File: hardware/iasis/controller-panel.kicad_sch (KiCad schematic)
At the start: 23 parts, among them SW1171 PTS645SL50SMTR92LFS, U1171 SN74AHCT1G125DBVR, U1172 TCA6408ARGTR

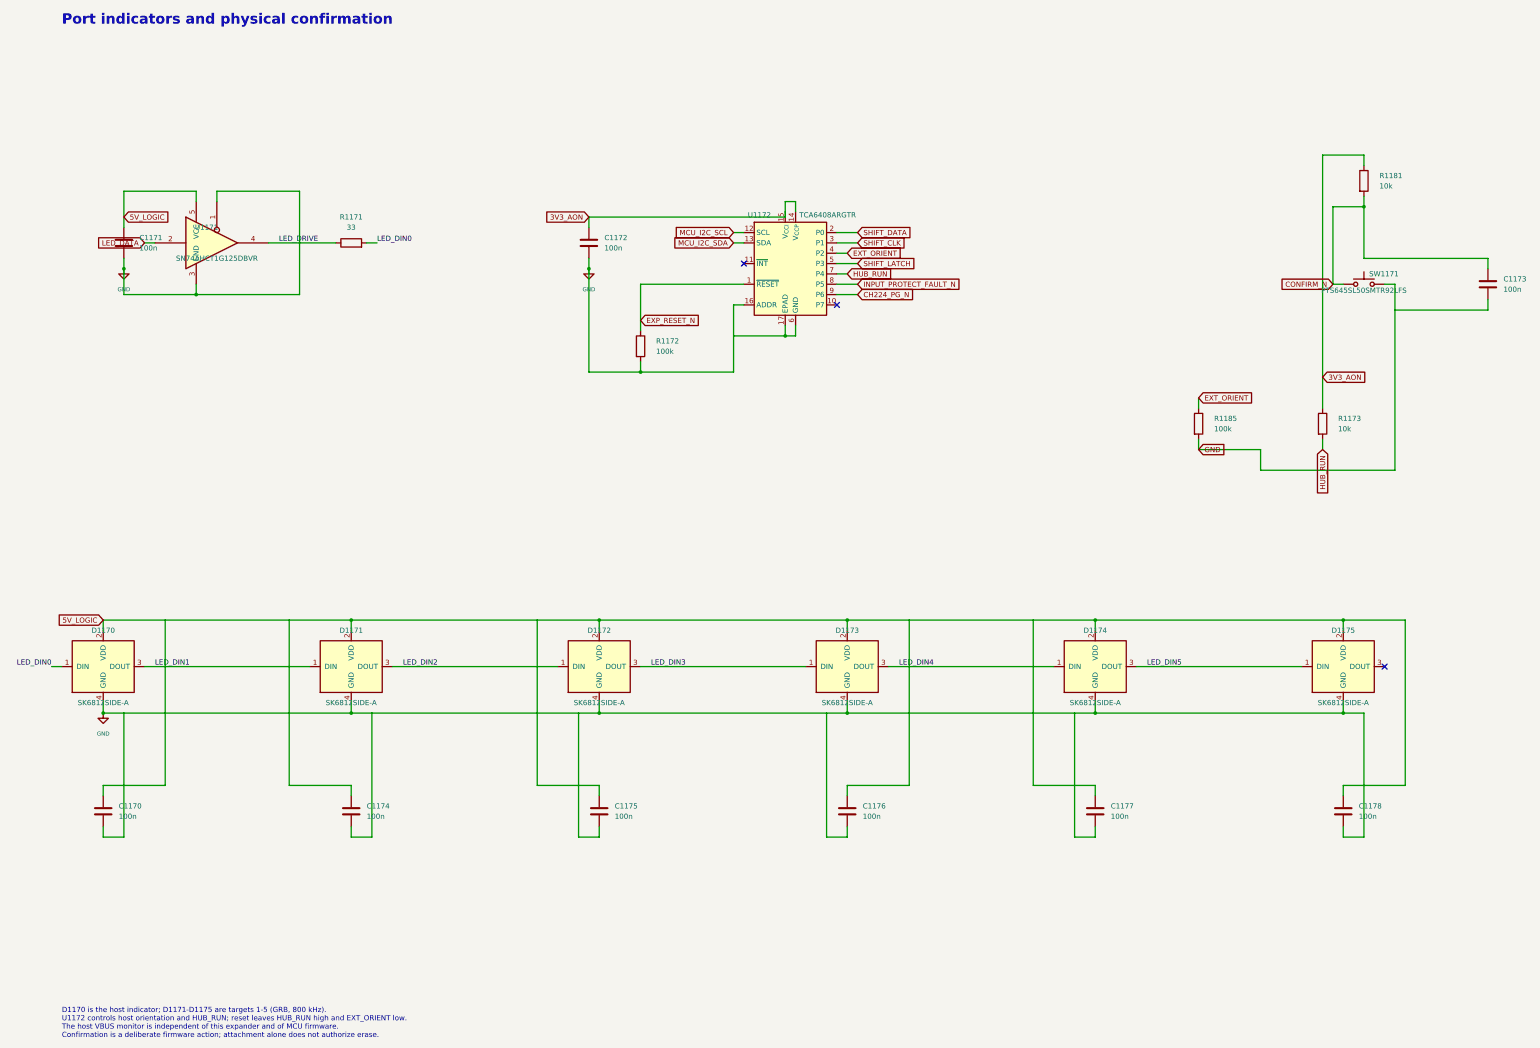
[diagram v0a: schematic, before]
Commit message: Wire the schematic islands and side-match the RP2354 GPIOs
Each sheet now draws its circuits with wires. Labels remain at block edges
and on single-part islands: buttons, test points, decoupling and pull
resistors. The target-port page wires its hierarchical labels straight to
the child sheet pins, the ports page points its labels away from each
block, and the root sheet keeps every block clear of the title block.

The RP2354B GPIOs are reassigned so each signal leaves the package on the
side facing its destination. Update PCB from Schematic applied the 43
U1101 pad-net changes with no geometry change. Otherwise the netlist
matches the previous design, ERC keeps its 14 existing warnings and DRC
reports no parity issues.
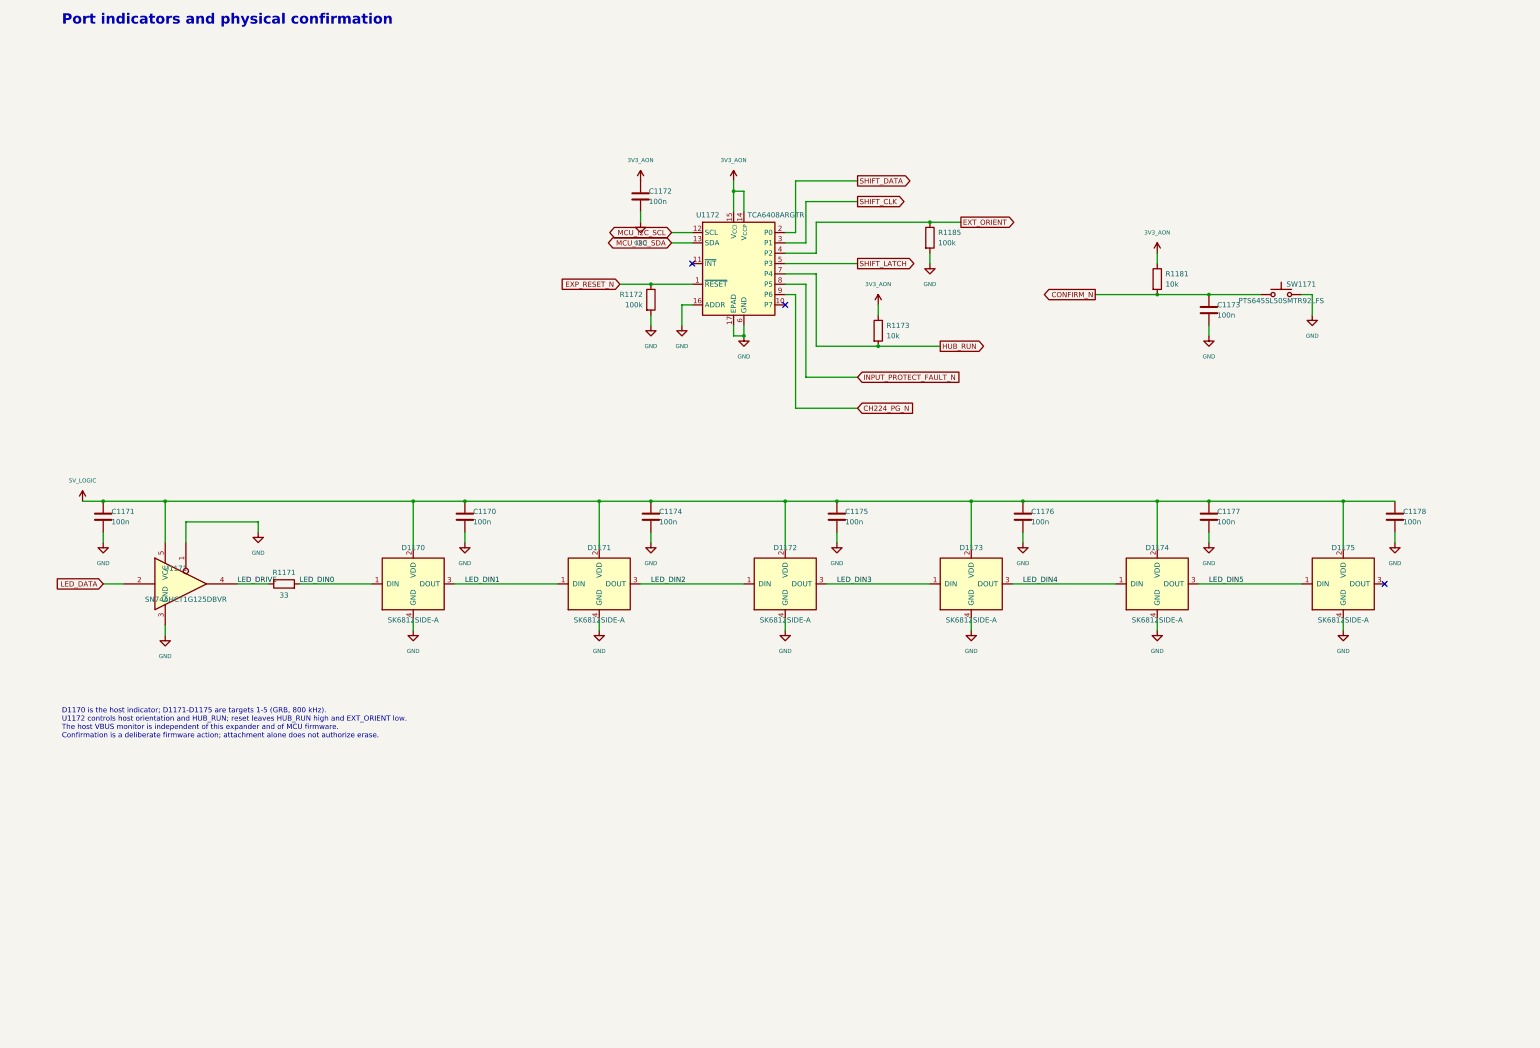
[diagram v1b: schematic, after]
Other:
- moved on the sheet: C1170, C1171, C1172, C1173, C1174, C1175, C1176, C1177, C1178, D1170, D1171, D1172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

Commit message: Redraw the controller support sheets
The management bus, indicator, power-control, voltage-measurement and
temperature sheets read left to right, with supplies up, ground down
and decoupling beside each IC. Pull resistors, test points and buttons
are labelled islands; everything else is wired. Supply rails use power
symbols with their existing net names, fields sit clear of bodies,
wires and text, and each sheet carries a title, date and revision. The
netlist is unchanged.
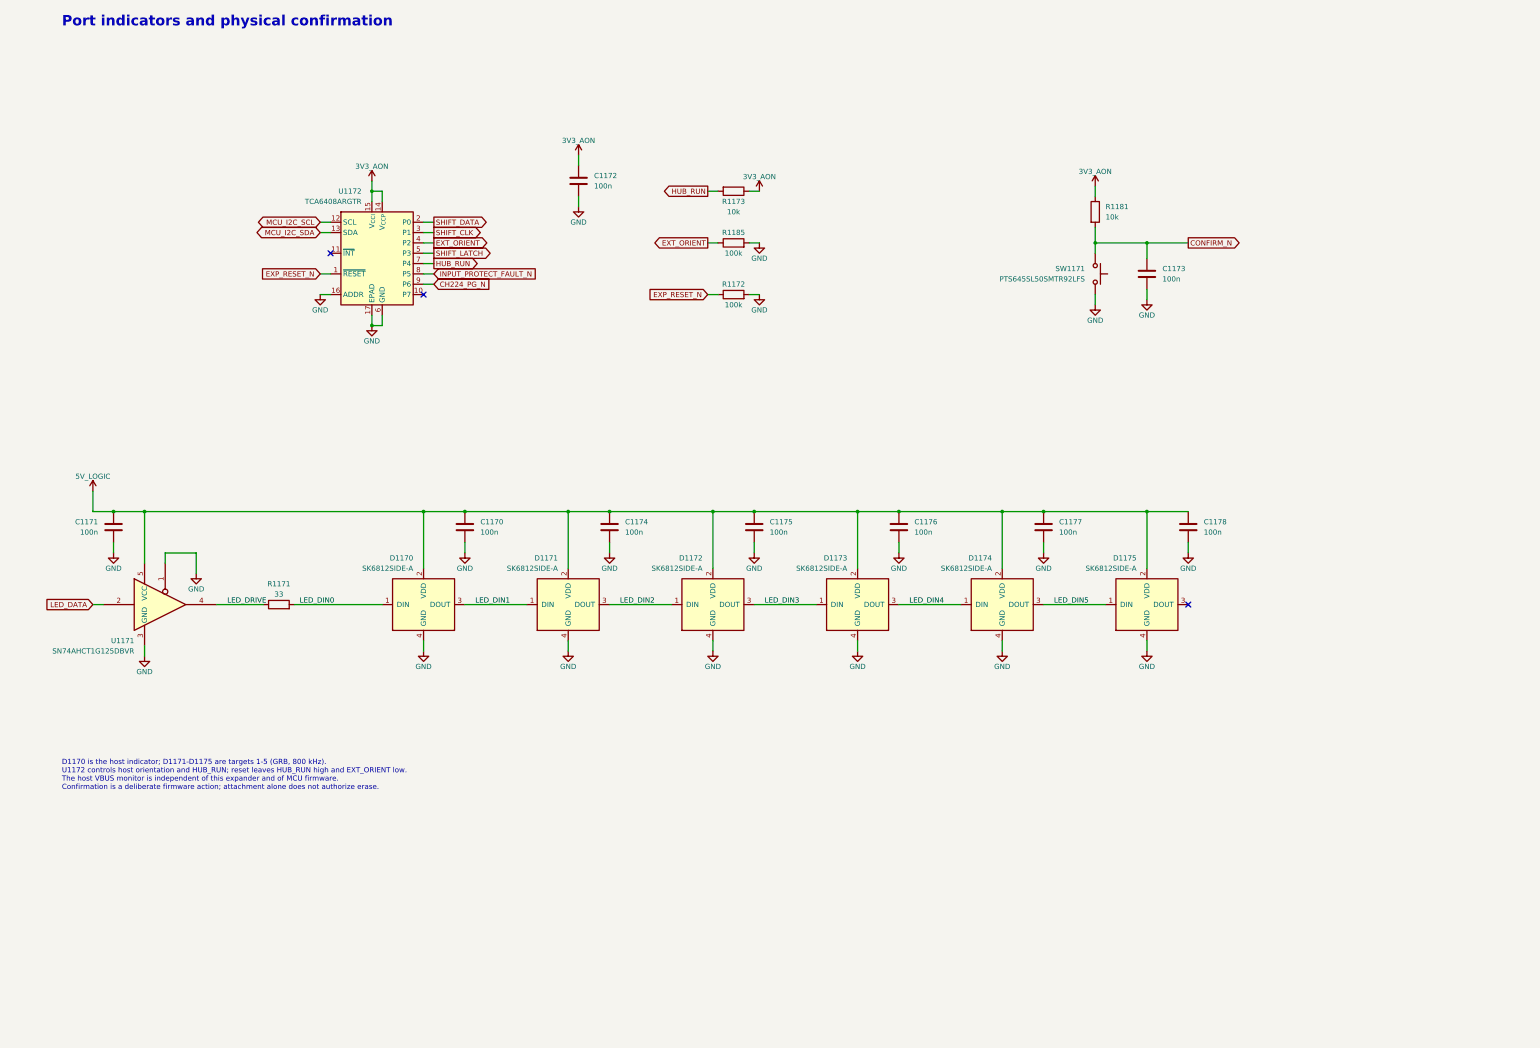
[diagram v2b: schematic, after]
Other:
- title: (none) -> Port indicators and physical confirmation
- moved on the sheet: C1170, C1171, C1172, C1173, C1174, C1175, C1176, C1177, C1178, D1170, D1171, D1172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

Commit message: Reassign RP2354 GPIOs by package side and reorder the LED chain
With the controller turned 90 degrees, charge-cell requests and faults
leave the top, upper-right and left of the package towards the charging
row, and the data-cell lines (orientation, PD interrupt, CC fault) leave
the bottom in port order. ADC channels stay on GPIO40-47, UART on
GPIO0/1, I2C on GPIO24/25.

The SK6812 chain now runs from the host LED at the front right through
ports 5 to 1, matching the board. Update PCB also adds the Hub-variant
DNP flags the swapped charging inductors and capacitors were missing.
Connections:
- net LED_DIN1: now also D1175.1 (DIN); no longer D1171.1 (DIN)
- net LED_DIN2: now also D1174.1 (DIN), D1175.3 (DOUT); no longer D1171.3 (DOUT), D1172.1 (DIN)
- net LED_DIN3: now also D1174.3 (DOUT); no longer D1172.3 (DOUT)
- net LED_DIN4: now also D1172.1 (DIN); no longer D1174.1 (DIN)
- net LED_DIN5: now also D1171.1 (DIN), D1172.3 (DOUT); no longer D1174.3 (DOUT), D1175.1 (DIN)
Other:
- moved on the sheet: C1174, C1175, C1177, C1178, D1171, D1172, D1174, D1175

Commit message: Keep the switch jumper flag in the symbol
Update PCB from Schematic sets each footprint's duplicate-pad jumper flag
from its symbol, so the flag set only on the SW1101, SW1102 and SW1171
footprints would not have survived the next update from the stock
Switch:SW_Push. The switches now use Iasis:PTS645SL50SMTR92LFS, SW_Push with
duplicate pin numbers marked as jumpers, and the netlist carries the flag to
the footprints.

The footprints stay stock. Update Footprints from Library takes the
library's flag, so after refreshing them DRC reports the three pads
unconnected until the next update from the schematic.

ERC is unchanged; DRC is clean with schematic parity.
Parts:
- SW1171: symbol Switch:SW_Push -> Iasis:PTS645SL50SMTR92LFS
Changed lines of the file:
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@@
 	)
 	(symbol
-		(lib_id "Switch:SW_Push")
+		(lib_id "Iasis:PTS645SL50SMTR92LFS")
 		(at 279.4 83.82 270)
 		(unit 1)
